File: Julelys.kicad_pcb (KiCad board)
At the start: 4 copper layers, 65 x 56 mm, 138 parts, among them J1 Raspberry_Pi_40pin, J10 B3B-XH-A, J11 B3B-XH-A, J12 Conn_01x03_Pin, J4 B3B-XH-A, J5 B3B-XH-A, J6 B3B-XH-A, J7 B3B-XH-A, J8 B3B-XH-A, J9 B3B-XH-A, P1 USB_C_Receptacle_USB2.0, SW1 SW_Push, SW2 SW_Push, U1 ESP32-C3FH4, U11 SRV05-4, U12 SRV05-4, U2 74HC4051, U3 AMS1117-3.3, U6 74AHCT1G125, U7 74AHCT1G125, U8 74AHCT1G125, U9 74AHCT1G125, Y1 40MHz

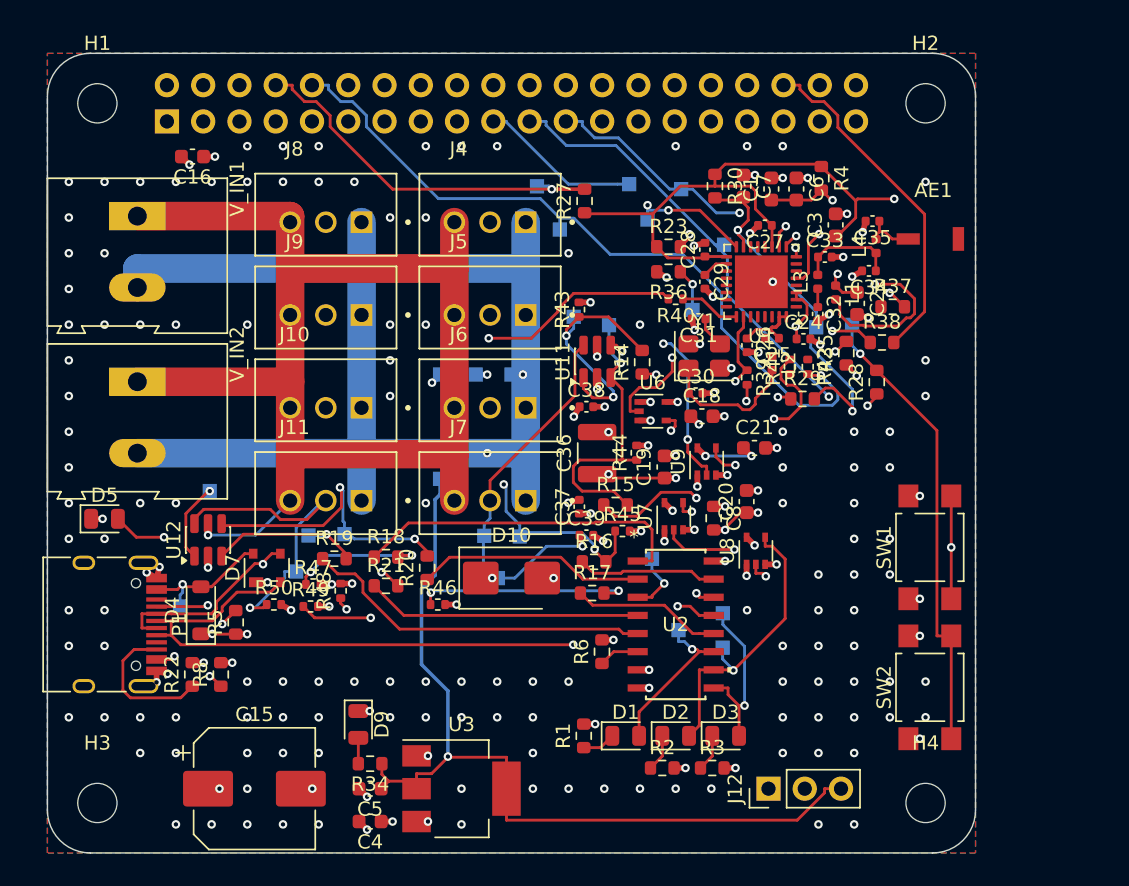
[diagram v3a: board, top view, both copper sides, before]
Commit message: Test board: level shifters and LED protection in rows
- U6-U9 in one row with C18-C21 below each VCC pin; C8 back at U2 pin 16.
- U12, R47-R50, R43-R46, U11 in one row under the JST columns, each TVS
  under its own channels. Pull-down GND pads face down and share a GND bus.
- Re-routed the CH/MCH nets around the rows; removed dangling vias/stubs.
- 0 DRC errors; 13 connections left, all at the QFN (hand fan-out).

Co-Authored-By: Claude Opus 5.5 <noreply@anthropic.com>
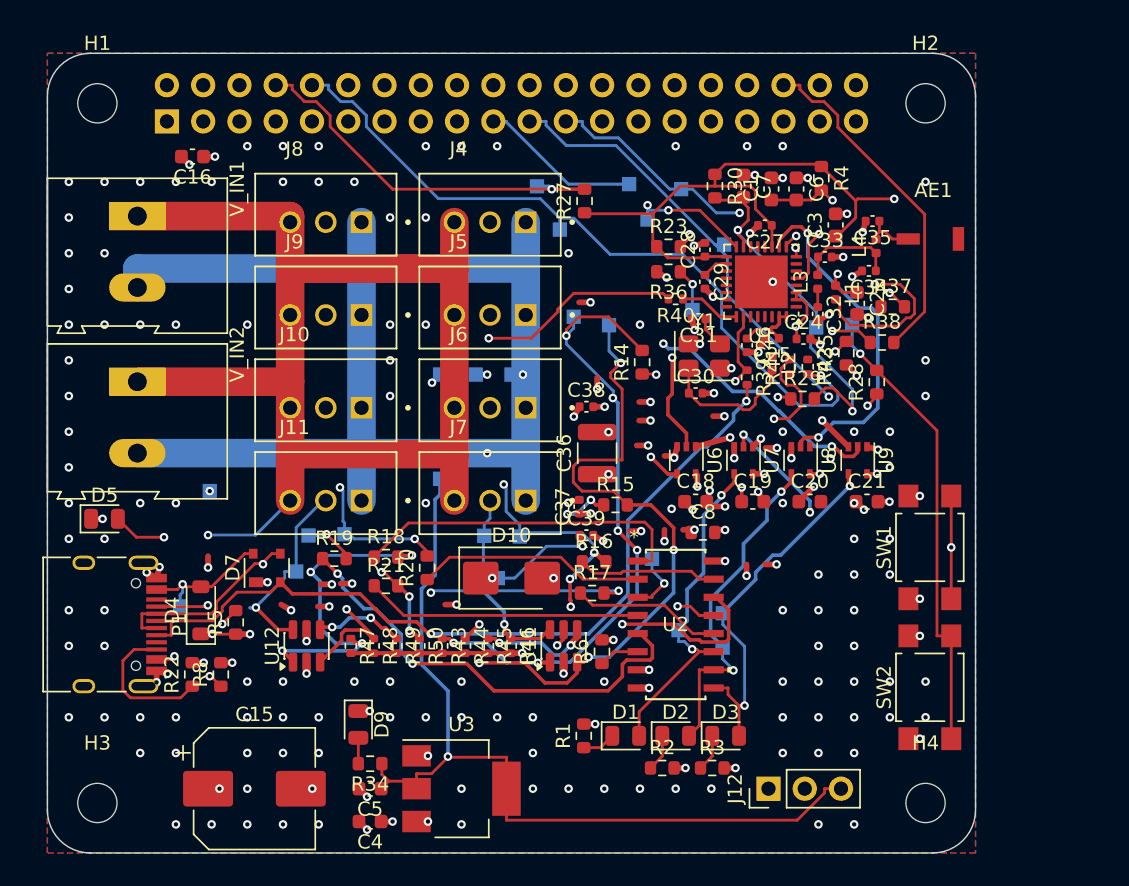
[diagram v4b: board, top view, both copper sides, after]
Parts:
- moved R43 25.4 mm to (47.6, 53.5), turned to -90 degrees
- moved U11 20.1 mm to (56.1, 53.5)
- moved R44 18.1 mm to (49.2, 53.5), turned to -90 degrees
- moved R45 12.4 mm to (50.9, 53.5), turned to -90 degrees
- moved R50 10.6 mm to (46.0, 53.5), turned to -90 degrees
- moved U9 10.6 mm to (76.8, 40.5), turned to -90 degrees
- moved U12 10.1 mm to (38.1, 53.5)
- moved C21 8.73 mm to (77.4, 43.4)
- moved U8 7.07 mm to (72.8, 40.5), turned to -90 degrees
- moved C19 6.64 mm to (69.4, 43.4), turned to 0 degrees
- moved R49 6.62 mm to (44.5, 53.5), turned to -90 degrees
- moved U7 6.26 mm to (68.8, 40.5), turned to -90 degrees
- moved C18 6.00 mm to (65.4, 43.4)
- moved R46 5.87 mm to (52.5, 53.5), turned to -90 degrees
- moved R47 5.05 mm to (41.2, 53.5), turned to -90 degrees
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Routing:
- net /CH1: track 27.6 -> 57.4 mm, vias 2 -> 6
- net /CH2: track 31.1 -> 60.0 mm, vias 1 -> 5
- net GND: track 155.6 -> 180.8 mm, vias 201 -> 205
- net A1: track 3.04 -> 24.7 mm
- net USB_D+: track 72.3 -> 57.4 mm
- net /CH5: track 46.8 -> 56.8 mm, vias 3 -> 5
- net /CH7: track 38.4 -> 30.1 mm, vias 3 -> 4
- net /MCH2: track 16.1 -> 23.9 mm, vias 2 -> 3
- net /CH4: track 35.7 -> 28.4 mm, vias 2 -> 3
- net /MCH6: track 24.7 -> 31.8 mm, vias 0 -> 2
- net /AS2: track 33.1 -> 26.0 mm
- net A2: track 20.8 -> 27.3 mm
- net +5V: track 217.9 -> 211.9 mm
- net /CH8: track 30.6 -> 27.0 mm, vias 2 -> 4
- net /AS1: track 20.9 -> 24.1 mm, vias 1 -> 2
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
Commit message: Test board: move protection parts and C36, reroute USB away from LEDs
- C36 (Pi bulk) now 100uF 1206, 5 mm from J1 pins 2/4 (was 39 mm).
- U11 next to the J4-J7 column, U12 below the V_IN terminals, D10 closer to V_IN.
- R40 beside R39 under U1; USB D+/D- rerouted below the JST block.
- CH nets rerouted; maze now checks every layer when placing vias.
- Noise analysis updated with the re-measured values.

Co-Authored-By: Claude Opus 5.5 <noreply@anthropic.com>
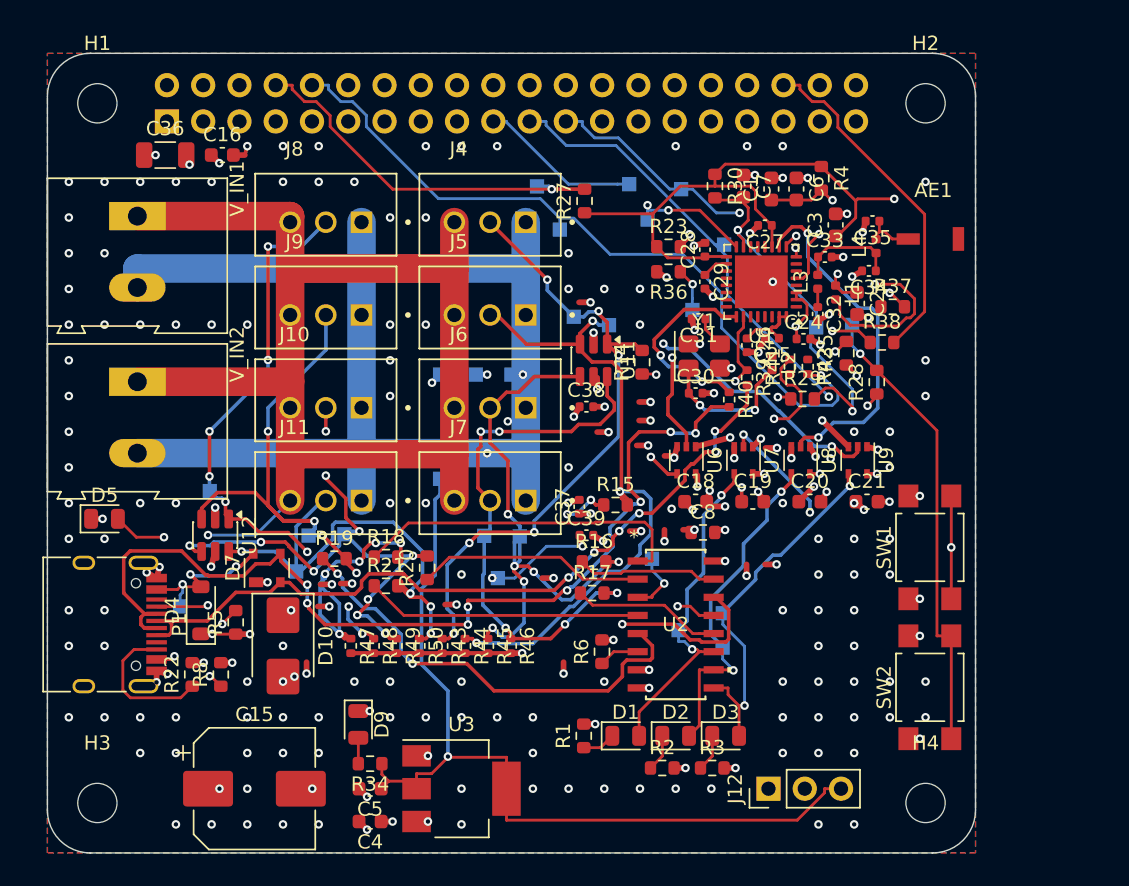
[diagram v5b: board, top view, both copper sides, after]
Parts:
- C36: footprint Capacitor_SMD:C_1210_3225Metric -> Capacitor_SMD:C_1206_3216Metric
- moved C36 36.8 mm to (28.2, 19.1), turned to 0 degrees
- moved U11 20.1 mm to (58.2, 33.5), turned to -90 degrees
- moved D10 16.7 mm to (36.5, 53.5), turned to -90 degrees
- moved U12 10.1 mm to (31.8, 45.8), turned to -90 degrees
- moved R40 7.99 mm to (67.8, 36.2), turned to -90 degrees
- moved C16 2.09 mm to (32.2, 19.1), turned to 0 degrees
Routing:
- net /CH2: track 60.0 -> 46.6 mm, vias 5 -> 3
- net /CH1: track 57.4 -> 45.1 mm
- net /CH7: track 30.1 -> 42.1 mm, vias 4 -> 10
- net /ESP32/U_DM: track 4.26 -> 14.1 mm, vias 0 -> 2
- net /CH4: track 28.4 -> 38.2 mm, vias 3 -> 5
- net USB_D-: track 59.3 -> 68.1 mm, vias 2 -> 8
- net /CH6: track 34.6 -> 42.1 mm, vias 2 -> 6
- net /CH8: track 27.0 -> 33.2 mm
- net /CH3: track 35.3 -> 40.0 mm
- net GND: track 180.8 -> 183.7 mm, vias 205 -> 216
- net /CH5: track 56.8 -> 54.1 mm, vias 5 -> 11
- net /ESP32/XTAL_PX: track 9.93 -> 11.9 mm, vias 0 -> 2
- net USB_D+: track 57.4 -> 55.4 mm, vias 2 -> 6
- net VBUS: track 16.2 -> 17.8 mm, vias 2 -> 4
- net +5V: track 211.9 -> 212.5 mm, vias 26 -> 27

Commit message: Test board: route the ESP32-C3 QFN fan-out, board fully routed
- Re-placed the parts around U1 so every pin can escape: RF chain straight
  out of pin 1, crystal below pins 29/30, decoupling at the pins, EN caps and
  A2/IO7 pull-ups moved out of the fan-out area, TP5/TP9 moved onto their nets.
- Fan-out: 0.15 mm tracks; rule area QFN_FAN with 0.15 mm clearance.
- RF and antenna feed 0.33 mm on F.Cu, no vias.
- 0 DRC errors, 0 unconnected, no dangling copper.

Co-Authored-By: Claude Opus 5.5 <noreply@anthropic.com>
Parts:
- moved R23 18.6 mm to (77.5, 37.9), turned to 180 degrees
- moved R36 10.6 mm to (64.0, 37.9)
- moved C30 8.83 mm to (74.1, 34.3), turned to -90 degrees
- moved C31 8.21 mm to (70.2, 37.4), turned to 0 degrees
- moved R41 7.59 mm to (64.8, 31.7), turned to 0 degrees
- moved R42 7.57 mm to (65.8, 33.0), turned to 180 degrees
- moved R40 6.48 mm to (66.2, 29.9), turned to 90 degrees
- moved Y1 5.60 mm to (71.3, 35.0), turned to 180 degrees
- moved C2 4.89 mm to (80.8, 32.2)
- moved C26 4.71 mm to (73.7, 32.2)
- moved C33 4.58 mm to (76.8, 30.2), turned to -90 degrees
- moved TP5 4.54 mm to (63.6, 27.9)
- moved C24 4.32 mm to (75.0, 28.2), turned to 90 degrees
- moved R39 3.75 mm to (66.8, 31.7), turned to 180 degrees
- moved TP9 3.70 mm to (72.0, 34.4)
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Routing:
- net /ESP32/VDD3P3: track 41.4 -> 4.48 mm, vias 2 -> 0
- net RXD: track 28.7 -> 60.2 mm, vias 1 -> 4
- net +3.3V: track 160.0 -> 176.7 mm, vias 4 -> 20
- net TXD: track 52.3 -> 36.1 mm
- net A2: track 27.3 -> 42.7 mm, vias 3 -> 2
- net IO2: track 35.7 -> 50.7 mm, vias 2 -> 6
- net IO6: track 11.4 -> 24.9 mm, vias 0 -> 1
- net /ESP32/U_DM: track 14.1 -> 2.70 mm, vias 2 -> 0
- net IO7: track 15.7 -> 26.2 mm
- net IO9: track 45.9 -> 56.0 mm, vias 3 -> 4
- net /ESP32/U_DP: track 15.8 -> 5.85 mm, vias 2 -> 0
- net PI_EN: track 36.8 -> 27.8 mm, vias 1 -> 2
- net /ESP32/XTAL_PX: track 11.9 -> 3.77 mm, vias 2 -> 0
- net IO0: track 0.00 -> 7.52 mm, vias 0 -> 2
- net USB_D+: track 55.4 -> 62.0 mm
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
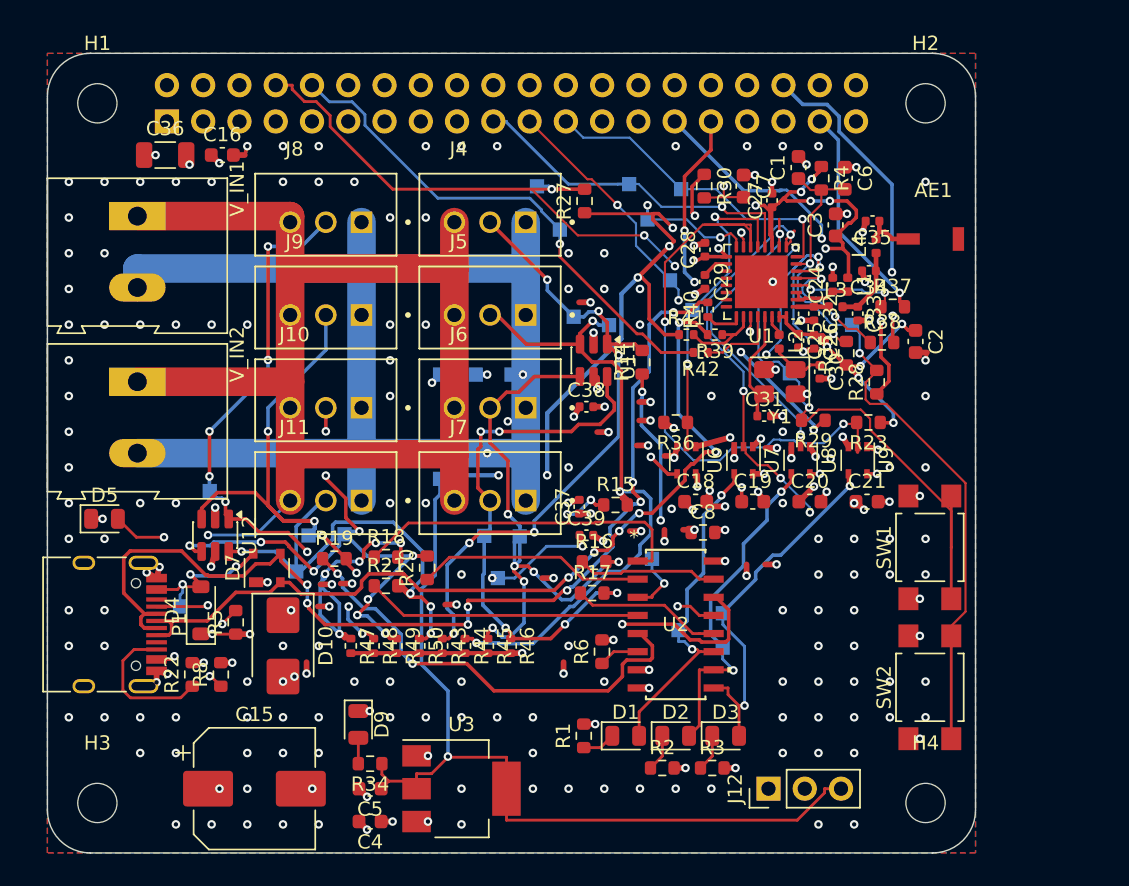
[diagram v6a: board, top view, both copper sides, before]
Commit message: Test board: clean up silkscreen
- Re-placed all reference texts (1.0 mm / 0.15 mm) clear of pads, silk and
  each other; hid C24-C26, C30-C34, C38 (no room in the RF area) and H1-H4.
- Removed footprint silk lines that touched pads or the board edge, and the
  duplicate pin-1 text on U2.
- Bottom: moved TP9 off the pinout table, the logo off J12, made the
  Boltehus text heavy enough to print, spaced the J1 37/36 label.
- 0 silkscreen warnings, 0 DRC errors, 0 unconnected.

Co-Authored-By: Claude Opus 5.5 <noreply@anthropic.com>
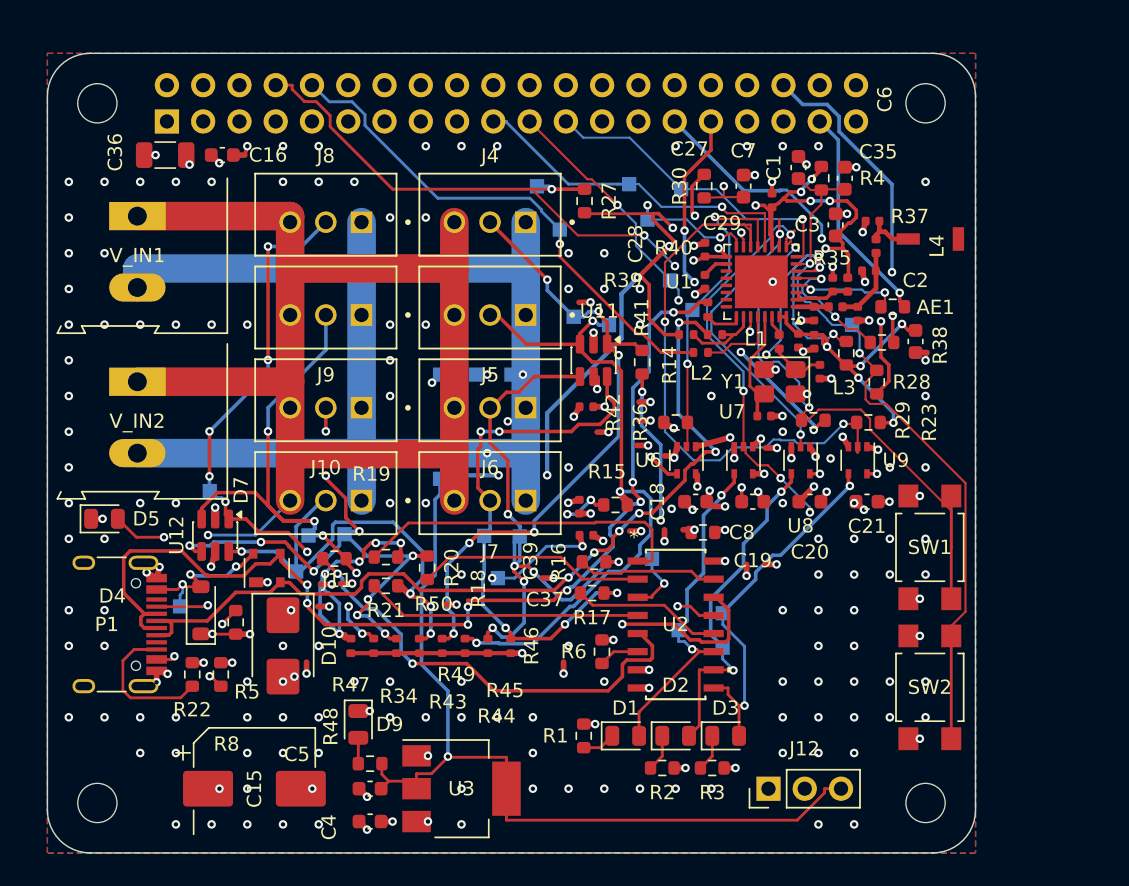
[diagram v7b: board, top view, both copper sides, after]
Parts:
- moved TP9 5.83 mm to (69.8, 29.0)
